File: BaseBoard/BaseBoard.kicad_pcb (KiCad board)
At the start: 4 copper layers, 50 x 35 mm, 45 parts, among them J1 locked, J2 Serial Port, J3 base connector, Q1 PMN48XP, SW2 boot, SW3 Reset, U1 ESP32-WROOM-E, U3 MCP73831-2ACI-OT, U4 XC6210B332MR

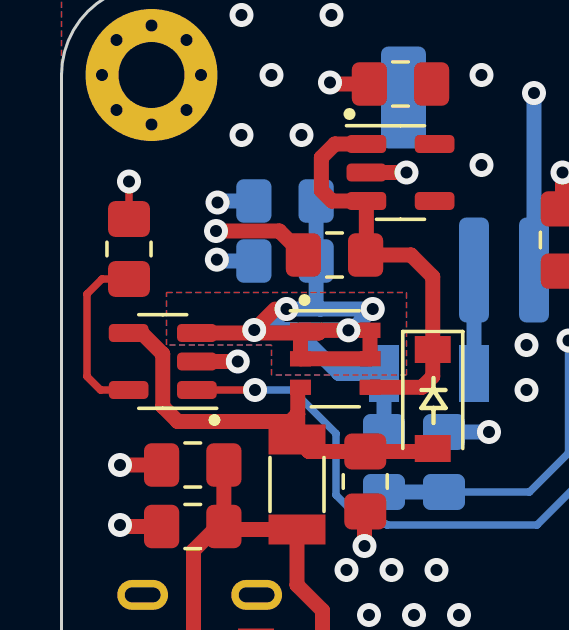
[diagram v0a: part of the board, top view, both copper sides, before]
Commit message: Updates base board revision label to 0.2
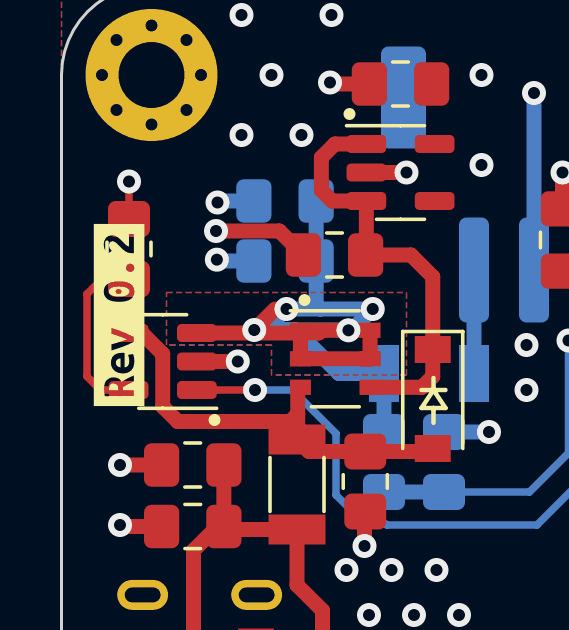
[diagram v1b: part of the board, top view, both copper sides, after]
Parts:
- removed kibuzzard-62599854: G***, kibuzzard-62599854
- added kibuzzard-62829F6C: G***, kibuzzard-62829F6C, F.Cu at (121.9, 91.0)

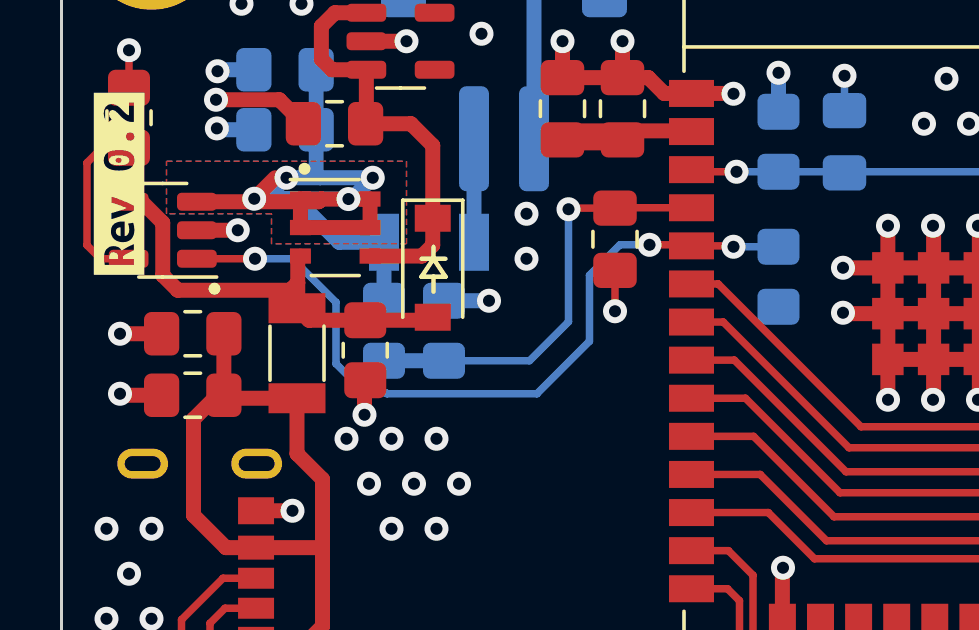
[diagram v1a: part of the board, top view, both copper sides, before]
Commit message: Fixes issue with battery status input
The battery status will be pulled high by the MCP73831 to it's VDD (5V)
when charging is done. This is higher than the 3.3V (+0.3V) allowed as
input to the ESP32. By adding a voltage divider we bring this to a lower
level with which we can interface to the ESP32.

When no 5V or no battery is present, the pin will be floating, so this
pin should have a internal pull-up to make sure we read the value
correctly. An internal pull-up will mean we'll see a high value with any
of charge complete, no 5V input, or no battery, which means a high value
whenever not charging.

The 150k resistor adds to the BOM, but in conjunction with the 100k it
will bring the 5V down to 3V, which is a safe value to input to the
ESP32.
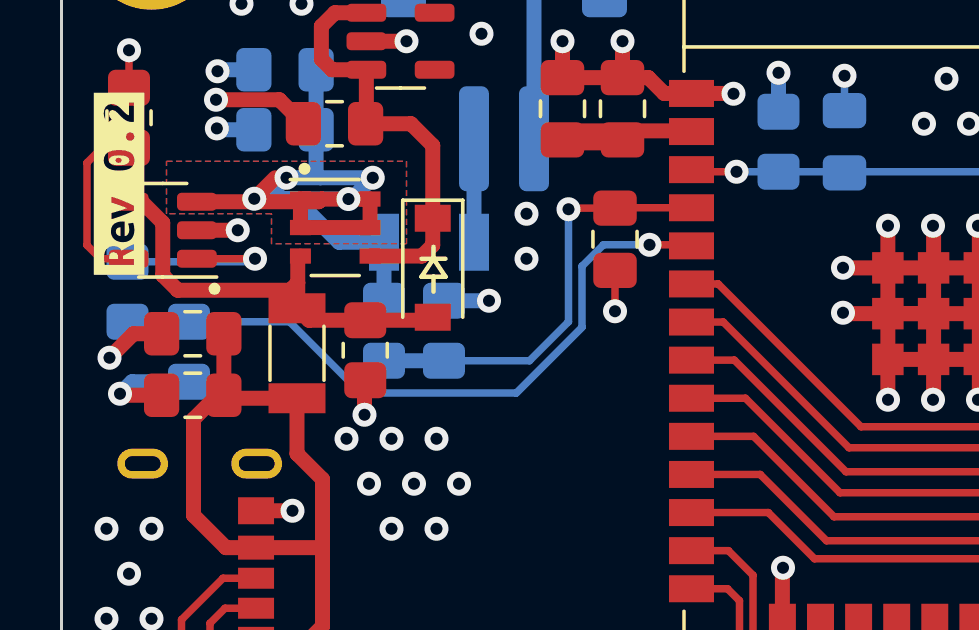
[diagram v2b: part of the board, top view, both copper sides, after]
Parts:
- added R13: 150kΩ, Resistor_SMD:R_0805_2012Metric_Pad1.20x1.40mm_HandSolder, B.Cu at (124.2, 96.6)
- R9: value 10kΩ -> 100kΩ
- moved R9 21.7 mm to (122.2, 94.6), turned to -90 degrees
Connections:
- R9 pad 1: +3V3 -> Net-(U3-STAT)
- U3 pad 1: BAT_STAT -> Net-(U3-STAT)
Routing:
- net Net-(U3-STAT): track 0.00 -> 6.23 mm, vias 0 -> 1
- net GND: track 96.6 -> 99.8 mm
- net BAT_STAT: track 25.8 -> 23.0 mm, vias 3 -> 1
- net Net-(J1-VBUS): track 24.2 -> 26.1 mm

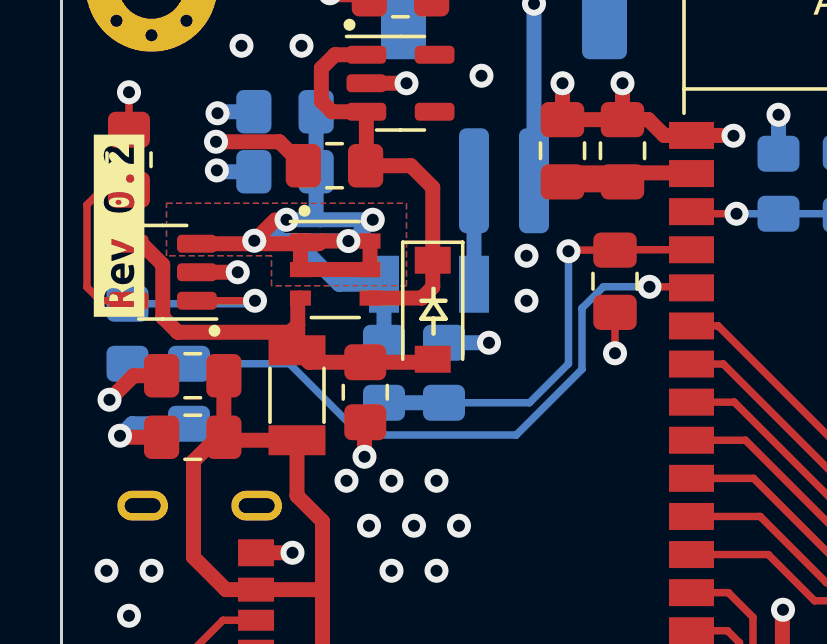
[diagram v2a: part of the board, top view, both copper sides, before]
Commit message: Adjusts alignment on 5v decoupling
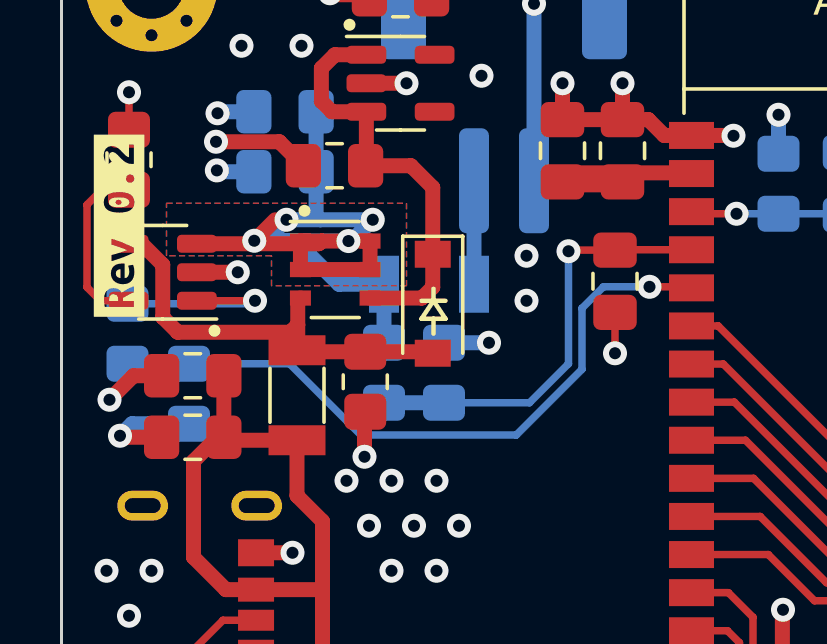
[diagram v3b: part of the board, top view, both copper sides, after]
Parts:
- moved R7 0.35 mm to (130.1, 96.2)
- moved D1 0.20 mm to (132.4, 93.6)
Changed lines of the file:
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@@
   )
   (footprint "Resistor_SMD:R_0805_2012Metric_Pad1.20x1.40mm_HandSolder" (layer "F.Cu")
-    (at 130.125 96.55 -90)
+    (at 130.125 96.2 -90)
     (descr "Resistor SMD 0805 (2012 Metric), square (rectangular) end terminal, IPC_7351 nominal with elongated pad for handsoldering. (Body size source: IPC-SM-782 page 72, https://www.pcb-3d.com/wordpress/wp-content/uploads/ipc-sm-782a_amendment_1_and_2.pdf), generated with kicad-footprint-generator")
     (tags "resistor handsolder")
@@
   )
   (footprint "Diode_SMD:D_SOD-123" (layer "F.Cu")
-    (at 132.375 93.8 -90)
+    (at 132.375 93.6 -90)
     (descr "SOD-123")
     (tags "SOD-123")
@@
   )
   (segment (start 133.75 92.95) (end 133.75 89.5) (width 0.5) (layer "B.Cu") (net 1))
+  (segment (start 130.1 98.7) (end 130.1 97.225) (width 0.5) (layer "F.Cu") (net 2))
   (segment (start 164.5 99.2) (end 164.5 99.534022) (width 0.25) (layer "F.Cu") (net 2))
   (segment (start 150.595 93.805) (end 150.595 96.855) (width 0.5) (layer "F.Cu") (net 2))
   (segment (start 151.945 93.805) (end 150.595 93.805) (width 0.5) (layer "F.Cu") (net 2))
+  (segment (start 130.1 97.225) (end 130.125 97.2) (width 0.5) (layer "F.Cu") (net 2))
   (segment (start 161.74 105.46) (end 163.15 105.46) (width 0.25) (layer "F.Cu") (net 2))
   (segment (start 139.5625 87.4625) (end 138.7 87.4625) (width 0.5) (layer "F.Cu") (net 2))
@@
   (segment (start 150.595 96.855) (end 151.895 96.855) (width 0.5) (layer "F.Cu") (net 2))
   (segment (start 163.79 94.46) (end 163.15 94.46) (width 0.25) (layer "F.Cu") (net 2))
-  (segment (start 130.1 97.575) (end 130.125 97.55) (width 0.5) (layer "F.Cu") (net 2))
   (segment (start 147.545 98.195) (end 147.545 96.855) (width 0.5) (layer "F.Cu") (net 2))
   (segment (start 122.25 86.55) (end 122.25 87.8) (width 0.25) (layer "F.Cu") (net 2))
@@
   (segment (start 121.55 113.15) (end 121.5 113.2) (width 0.25) (layer "F.Cu") (net 2))
   (segment (start 164.028848 86.77) (end 164.03171 86.77) (width 0.15) (layer "F.Cu") (net 2))
-  (segment (start 130.1 98.7) (end 130.1 97.575) (width 0.5) (layer "F.Cu") (net 2))
   (segment (start 146.055 93.805) (end 146.05 93.8) (width 0.5) (layer "F.Cu") (net 2))
   (segment (start 149.07 93.805) (end 149.07 96.855) (width 0.5) (layer "F.Cu") (net 2))
@@
   (segment (start 128.7 105.75) (end 128.7 103.1) (width 0.5) (layer "F.Cu") (net 7))
   (segment (start 124.4 102.05) (end 124.4 98.85) (width 0.5) (layer "F.Cu") (net 7))
-  (segment (start 130.285 93.41) (end 132.015 93.41) (width 0.5) (layer "F.Cu") (net 8))
-  (segment (start 132.375 93.05) (end 132.375 92.15) (width 0.5) (layer "F.Cu") (net 8))
-  (segment (start 132.375 89.725) (end 132.375 92.15) (width 0.5) (layer "F.Cu") (net 8))
+  (segment (start 131.65 89) (end 132.375 89.725) (width 0.5) (layer "F.Cu") (net 8))
+  (segment (start 132.375 89.725) (end 132.375 91.95) (width 0.5) (layer "F.Cu") (net 8))
   (segment (start 129.1125 85.3) (end 128.6625 85.75) (width 0.5) (layer "F.Cu") (net 8))
   (segment (start 130.1625 87.2) (end 130.1625 88.975) (width 0.5) (layer "F.Cu") (net 8))
+  (segment (start 130.285 93.41) (end 132.015 93.41) (width 0.5) (layer "F.Cu") (net 8))
   (segment (start 128.6625 85.75) (end 128.6625 86.85) (width 0.5) (layer "F.Cu") (net 8))
+  (segment (start 132.375 93.05) (end 132.375 91.95) (width 0.5) (layer "F.Cu") (net 8))
+  (segment (start 130.1625 85.3) (end 129.1125 85.3) (width 0.5) (layer "F.Cu") (net 8))
+  (segment (start 129.0125 87.2) (end 130.1625 87.2) (width 0.5) (layer "F.Cu") (net 8))
   (segment (start 132.015 93.41) (end 132.375 93.05) (width 0.5) (layer "F.Cu") (net 8))
-  (segment (start 131.65 89) (end 132.375 89.725) (width 0.5) (layer "F.Cu") (net 8))
-  (segment (start 130.1625 85.3) (end 129.1125 85.3) (width 0.5) (layer "F.Cu") (net 8))
+  (segment (start 128.6625 86.85) (end 129.0125 87.2) (width 0.5) (layer "F.Cu") (net 8))
   (segment (start 130.1375 89) (end 131.65 89) (width 0.5) (layer "F.Cu") (net 8))
-  (segment (start 129.0125 87.2) (end 130.1625 87.2) (width 0.5) (layer "F.Cu") (net 8))
-  (segment (start 128.6625 86.85) (end 129.0125 87.2) (width 0.5) (layer "F.Cu") (net 8))
   (segment (start 130.1625 88.975) (end 130.1375 89) (width 0.5) (layer "F.Cu") (net 8))
   (segment (start 128.575 91.6) (end 128.665 91.51) (width 0.5) (layer "F.Cu") (net 9))
@@
   (segment (start 129.665 91.51) (end 130.375 90.8) (width 0.5) (layer "B.Cu") (net 9))
   (segment (start 130.75 94.9) (end 130.75 92.95) (width 0.5) (layer "B.Cu") (net 9))
-  (segment (start 128.25 95.55) (end 130.125 95.55) (width 0.5) (layer "F.Cu") (net 10))
+  (segment (start 132.325 95.2) (end 132.375 95.25) (width 0.5) (layer "F.Cu") (net 10))
   (segment (start 122.2375 91.6) (end 122.675 91.6) (width 0.5) (layer "F.Cu") (net 10))
   (segment (start 123.375 92.3) (end 123.375 94.05) (width 0.5) (layer "F.Cu") (net 10))
-  (segment (start 130.125 95.55) (end 132.275 95.55) (width 0.5) (layer "F.Cu") (net 10))
-  (segment (start 127.85 95.15) (end 128.25 95.55) (width 0.5) (layer "F.Cu") (net 10))
+  (segment (start 130.125 95.2) (end 132.325 95.2) (width 0.5) (layer "F.Cu") (net 10))
   (segment (start 127.85 95.15) (end 127.875 95.125) (width 0.5) (layer "F.Cu") (net 10))
   (segment (start 123.375 94.05) (end 123.875 94.55) (width 0.5) (layer "F.Cu") (net 10))
@@
   (segment (start 122.675 91.6) (end 123.375 92.3) (width 0.5) (layer "F.Cu") (net 10))
   (segment (start 127.875 93.5) (end 127.965 93.41) (width 0.5) (layer "F.Cu") (net 10))
+  (segment (start 127.9 95.2) (end 130.125 95.2) (width 0.5) (layer "F.Cu") (net 10))
   (segment (start 127.875 95.125) (end 127.875 94.3) (width 0.5) (layer "F.Cu") (net 10))
+  (segment (start 127.85 95.15) (end 127.9 95.2) (width 0.5) (layer "F.Cu") (net 10))
   (segment (start 123.875 94.55) (end 127.625 94.55) (width 0.5) (layer "F.Cu") (net 10))
   (segment (start 127.625 94.55) (end 127.875 94.3) (width 0.5) (layer "F.Cu") (net 10))
-  (segment (start 132.275 95.55) (end 132.375 95.45) (width 0.5) (layer "F.Cu") (net 10))
   (segment (start 146.7525 113.434368) (end 146.7525 110.6975) (width 0.2) (layer "F.Cu") (net 11))
   (segment (start 146.7525 110.6975) (end 146.95 110.5) (width 0.2) (layer "F.Cu") (net 11))

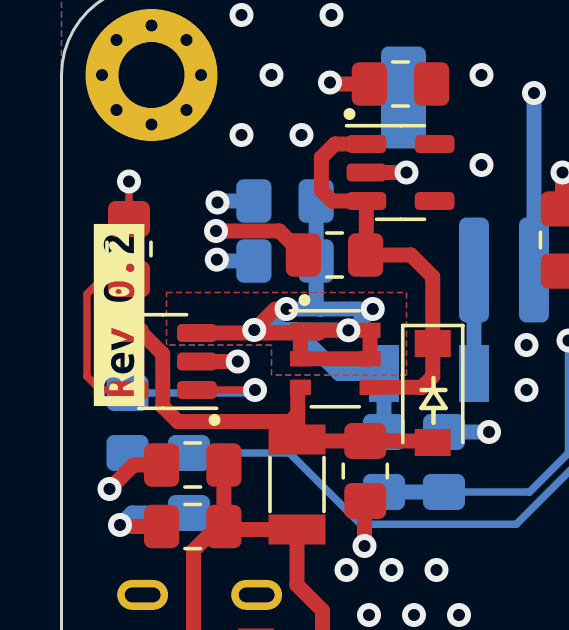
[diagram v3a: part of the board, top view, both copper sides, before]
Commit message: Moves revision number silkscreen on baseboard
After adding the new resistor it had no room left where it was.
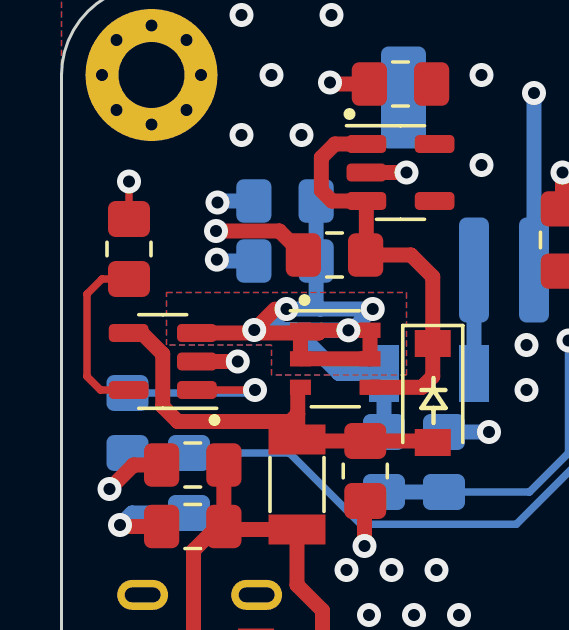
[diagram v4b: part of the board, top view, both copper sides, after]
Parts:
- kibuzzard-62829F6C: moved to B.Cu
- moved kibuzzard-62829F6C 25.3 mm to (133.6, 113.4), turned to 180 degrees
